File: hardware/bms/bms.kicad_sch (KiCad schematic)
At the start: 40 parts

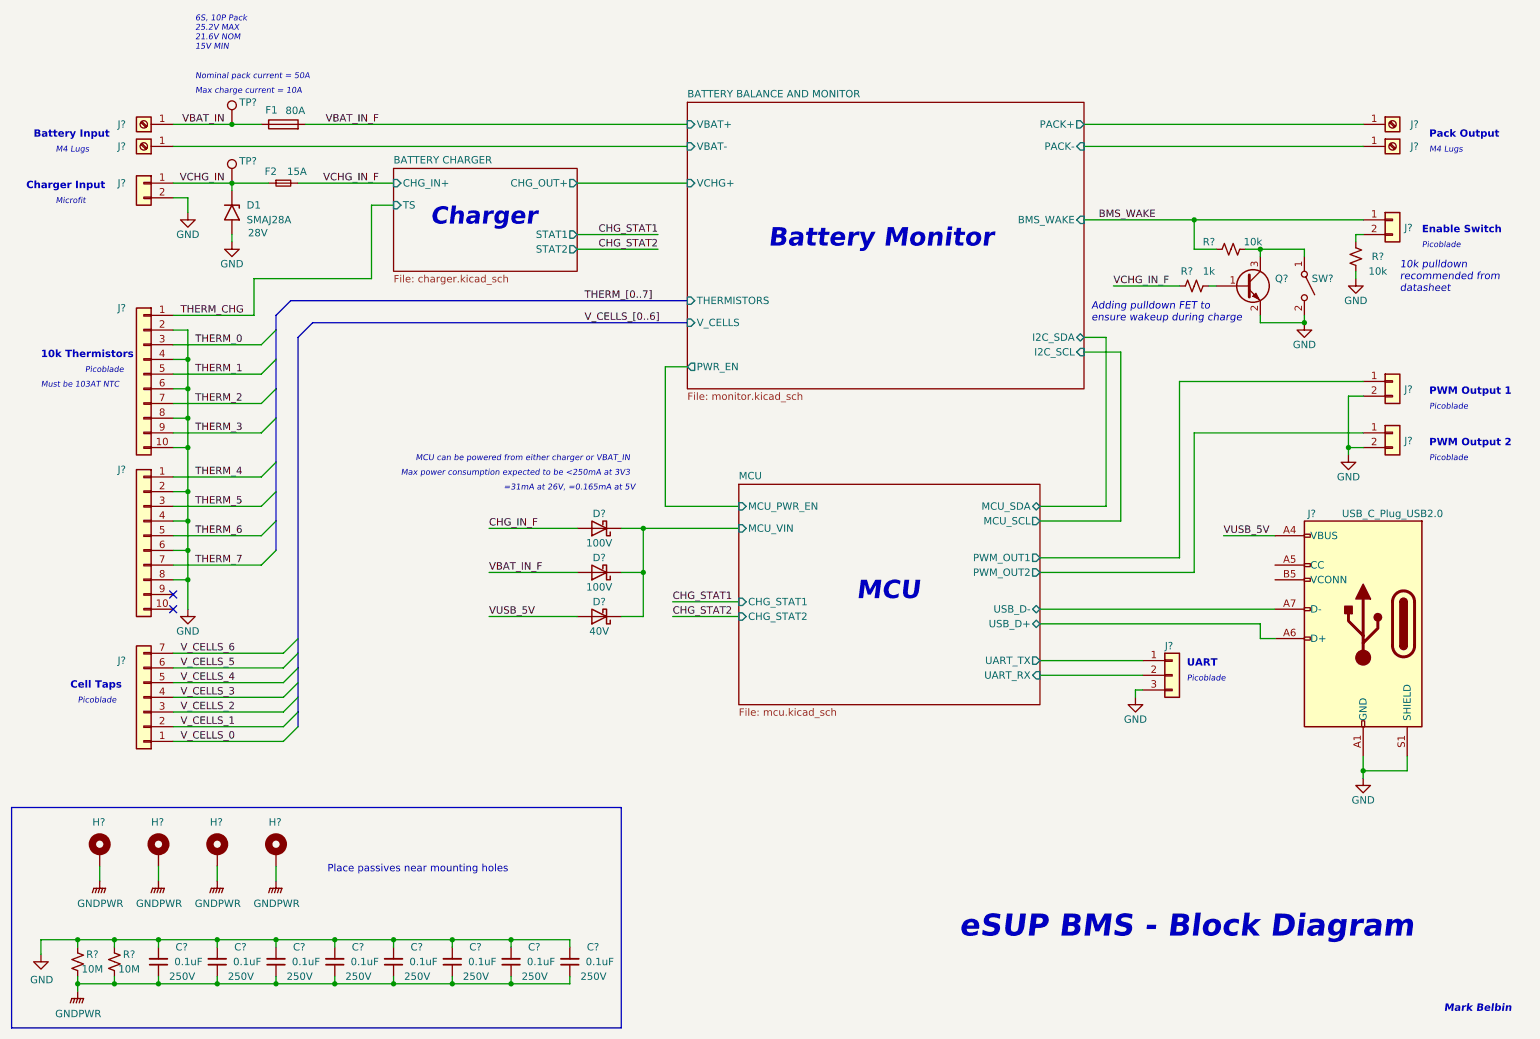
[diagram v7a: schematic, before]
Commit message: Selected power conversion scheme and converters.
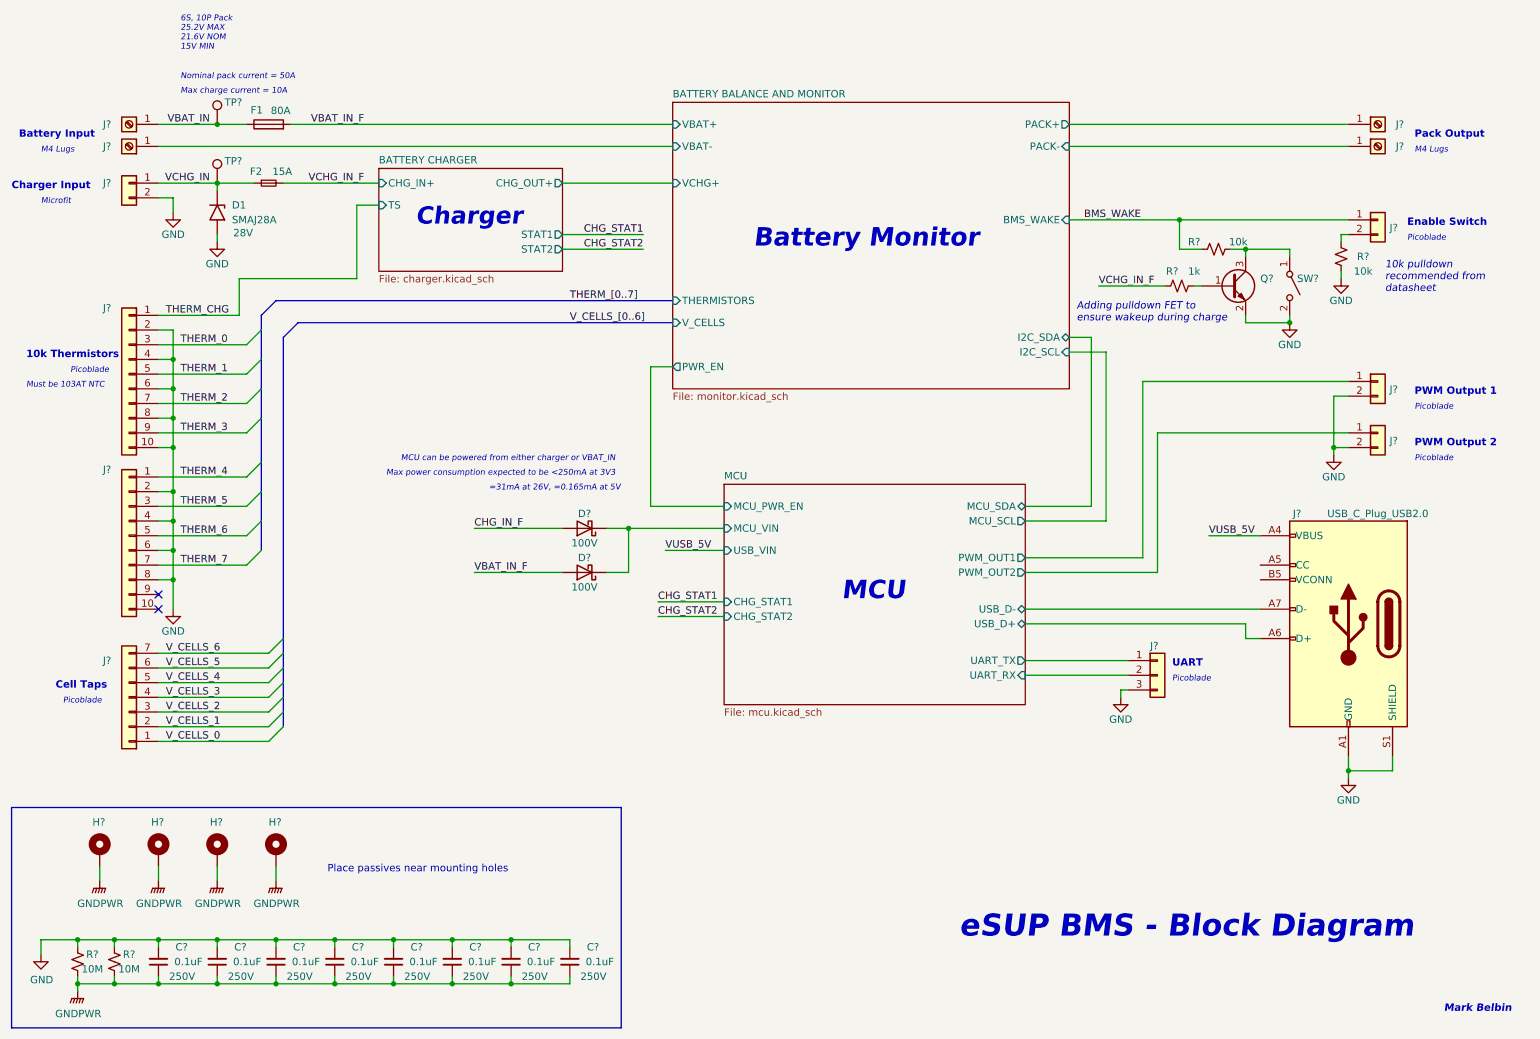
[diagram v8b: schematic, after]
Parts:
- removed D?: D_Schottky, Diode_SMD:D_SOD-123, symbol Device:D_Schottky
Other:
- sheet MCU ports: added USB_VIN; removed none
- moved on the sheet: D1, D?, F1, F2, J?, Q?, R?, SW?, TP?
